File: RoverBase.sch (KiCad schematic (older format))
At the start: 59 parts, among them J1 Conn_01x02, J2 Conn_01x06, J3 Conn_01x04, J4 Conn_01x02, J5 Conn_01x03, J6 Conn_02x03_Counter_Clockwise, J7 Conn_02x03_Counter_Clockwise, SW1 SW_SPDT, SW2 SW_SPDT, SW3 SW_SPDT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

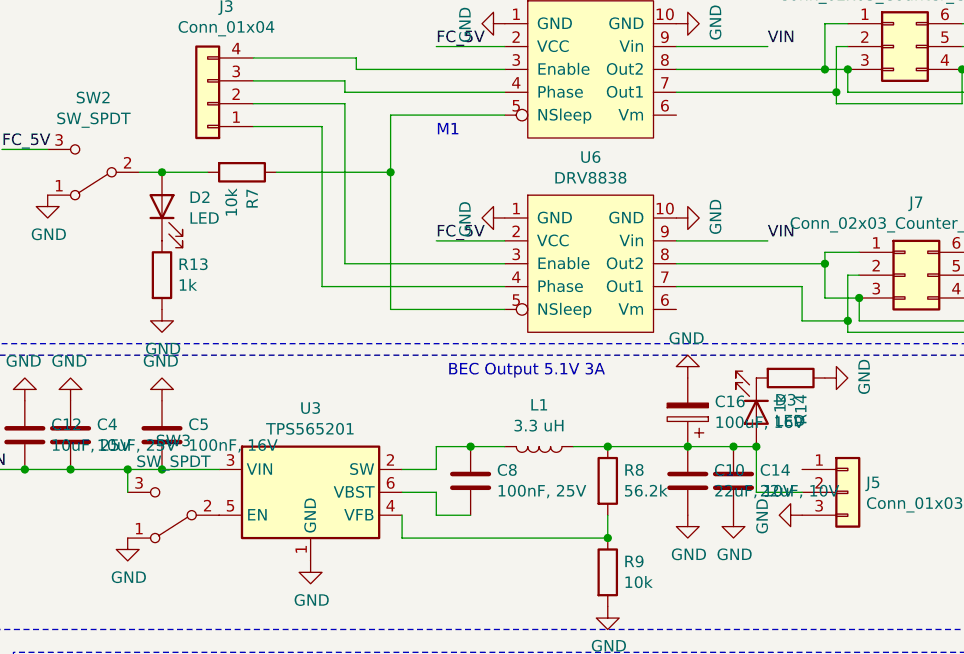
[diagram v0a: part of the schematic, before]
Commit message: Fixes from V1 testing
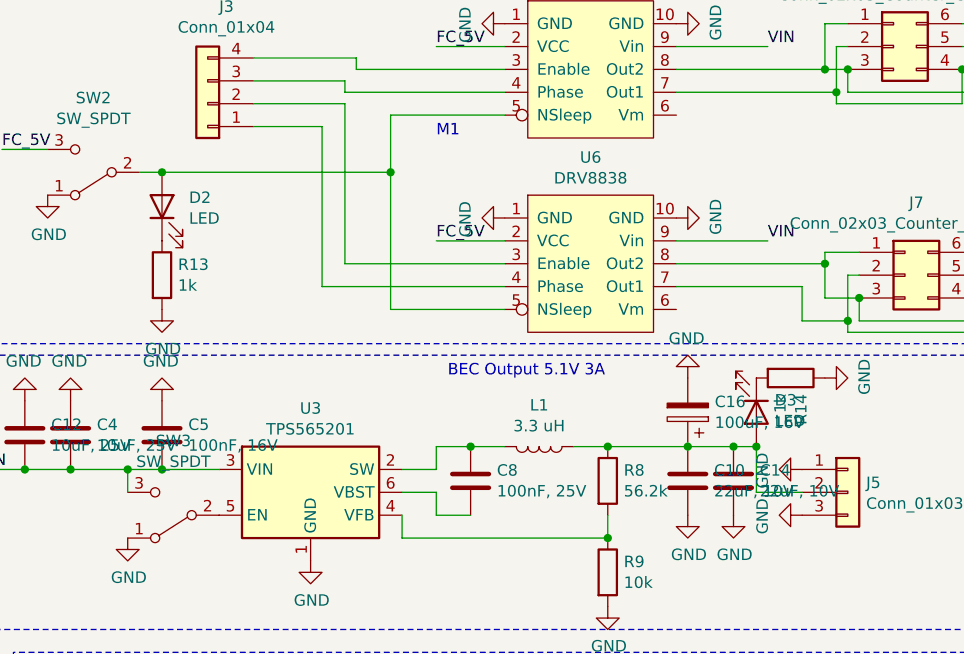
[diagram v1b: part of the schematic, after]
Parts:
- removed R7: 10k, Resistor_SMD:R_0402_1005Metric_Pad0.72x0.64mm_HandSolder, symbol Device:R
- H1, H2, H3, H4: footprint MountingHole:MountingHole_3.2mm_M3_ISO7380 -> MountingHole:MountingHole_3.5mm
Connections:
- net GND: now also J5.1 (Pin_1)
- net at U5.5 (NSleep), U6.5 (NSleep): now also D2.2 (A), SW2.2 (B)
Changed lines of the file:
@@
 Text Notes 3500 1100 0    50   ~ 0
 7A Limit
-$Comp
-L Device:R R7
-U 1 1 5FBF30CD
-P 7900 3900
-F 0 "R7" H 7970 3946 50  0000 L CNN
-F 1 "10k" H 7970 3855 50  0000 L CNN
-F 2 "Resistor_SMD:R_0402_1005Metric_Pad0.72x0.64mm_HandSolder" V 7830 3900 50  0001 C CNN
-F 3 "~" H 7900 3900 50  0001 C CNN
-F 4 "CRCW040210K0FKED" H 7900 3900 50  0001 C CNN "MPN"
-F 5 "541-3959-1-ND" H 7900 3900 50  0001 C CNN "SPN"
-	1    7900 3900
-	0    1    1    0
-$EndComp
 Wire Wire Line
 	8550 3650 8550 3900
 Wire Wire Line
 	7450 3900 7550 3900
-Wire Wire Line
-	8050 3900 8550 3900
 Connection ~ 8550 3900
 Wire Wire Line
@@
 $EndComp
 Connection ~ 7550 3900
-Wire Wire Line
-	7550 3900 7750 3900
 $Comp
 L Device:LED D3
@@
 F 0 "H1" H 1550 6146 50  0000 L CNN
 F 1 "MountingHole" H 1550 6055 50  0000 L CNN
-F 2 "MountingHole:MountingHole_3.2mm_M3_ISO7380" H 1450 6100 50  0001 C CNN
+F 2 "MountingHole:MountingHole_3.5mm" H 1450 6100 50  0001 C CNN
 F 3 "~" H 1450 6100 50  0001 C CNN
 F 4 "nf" H 1450 6100 50  0001 C CNN "MPN"
@@
 F 0 "H3" H 2350 6146 50  0000 L CNN
 F 1 "MountingHole" H 2350 6055 50  0000 L CNN
-F 2 "MountingHole:MountingHole_3.2mm_M3_ISO7380" H 2250 6100 50  0001 C CNN
+F 2 "MountingHole:MountingHole_3.5mm" H 2250 6100 50  0001 C CNN
 F 3 "~" H 2250 6100 50  0001 C CNN
 F 4 "nf" H 2250 6100 50  0001 C CNN "MPN"
@@
 F 0 "H4" H 2350 6546 50  0000 L CNN
 F 1 "MountingHole" H 2350 6455 50  0000 L CNN
-F 2 "MountingHole:MountingHole_3.2mm_M3_ISO7380" H 2250 6500 50  0001 C CNN
+F 2 "MountingHole:MountingHole_3.5mm" H 2250 6500 50  0001 C CNN
 F 3 "~" H 2250 6500 50  0001 C CNN
 F 4 "nf" H 2250 6500 50  0001 C CNN "MPN"
@@
 F 0 "H2" H 1550 6546 50  0000 L CNN
 F 1 "MountingHole" H 1550 6455 50  0000 L CNN
-F 2 "MountingHole:MountingHole_3.2mm_M3_ISO7380" H 1450 6500 50  0001 C CNN
+F 2 "MountingHole:MountingHole_3.5mm" H 1450 6500 50  0001 C CNN
 F 3 "~" H 1450 6500 50  0001 C CNN
 F 4 "nf" H 1450 6500 50  0001 C CNN "MPN"
@@
 	6150 2100 6350 2100
 Connection ~ 6350 2100
+Wire Wire Line
+	7550 3900 8550 3900
+$Comp
+L power:GND #PWR?
+U 1 1 5FFBA6CD
+P 10350 5200
+F 0 "#PWR?" H 10350 4950 50  0001 C CNN
+F 1 "GND" H 10355 5027 50  0000 C CNN
+F 2 "" H 10350 5200 50  0001 C CNN
+F 3 "" H 10350 5200 50  0001 C CNN
+	1    10350 5200
+	0    1    1    0
+$EndComp
 $EndSCHEMATC

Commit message: Updated inductor footprint
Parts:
- L1, L2: footprint Inductor_SMD:L_Vishay_IHLP-4040 -> Vishay_IHLP-3232:L_Vishay_IHLP-3232
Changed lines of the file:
@@
 F 0 "L2" V 9769 1600 50  0000 C CNN
 F 1 "3.3 uH" V 9860 1600 50  0000 C CNN
-F 2 "Inductor_SMD:L_Vishay_IHLP-4040" H 9950 1600 50  0001 C CNN
+F 2 "Vishay_IHLP-3232:L_Vishay_IHLP-3232" H 9950 1600 50  0001 C CNN
 F 3 "~" H 9950 1600 50  0001 C CNN
 F 4 "IHLP3232DZER3R3M01" H 9950 1600 50  0001 C CNN "MPN"
@@
 F 0 "L1" V 9019 5100 50  0000 C CNN
 F 1 "3.3 uH" V 9110 5100 50  0000 C CNN
-F 2 "Inductor_SMD:L_Vishay_IHLP-4040" H 9200 5100 50  0001 C CNN
+F 2 "Vishay_IHLP-3232:L_Vishay_IHLP-3232" H 9200 5100 50  0001 C CNN
 F 3 "~" H 9200 5100 50  0001 C CNN
 F 4 "IHLP3232DZER3R3M01" H 9200 5100 50  0001 C CNN "MPN"

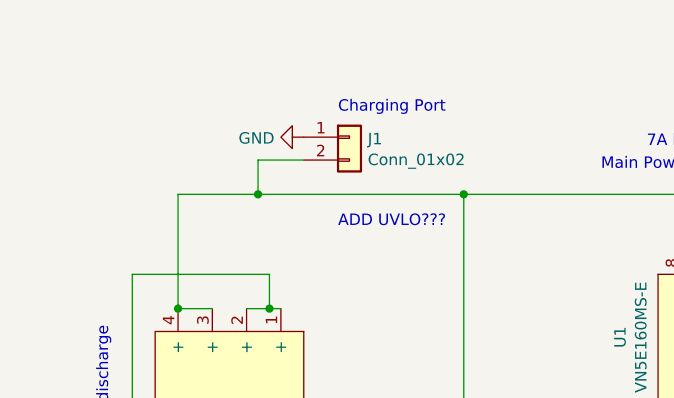
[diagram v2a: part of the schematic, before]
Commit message: Better power supply placement
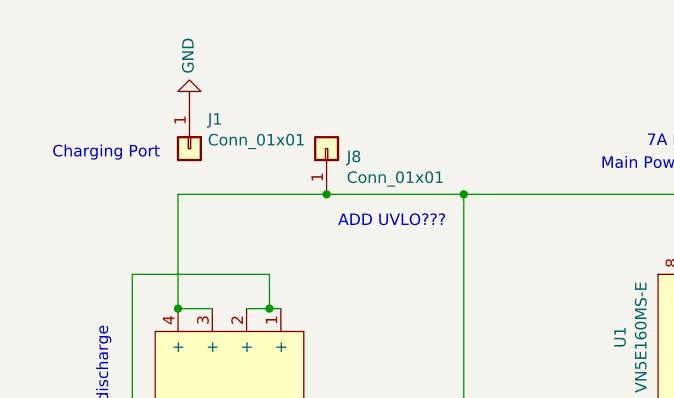
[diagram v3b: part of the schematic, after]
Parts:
- removed J1: Conn_01x02, Connector_PinHeader_2.54mm:PinHeader_1x02_P2.54mm_Vertical, symbol Connector_Generic:Conn_01x02
- added J1, J8: Conn_01x01, Connector_Pin:Pin_D1.3mm_L11.0mm, symbol Connector_Generic:Conn_01x01
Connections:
- net GND: now also J1.1 (Pin_1)
- net at BT1.3 (+), BT1.4 (+), R1.1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: now also J8.1 (Pin_1)
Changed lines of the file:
@@
 $EndDescr
-$Comp
-L Connector_Generic:Conn_01x02 J1
-U 1 1 5F777BC5
-P 2200 1050
-F 0 "J1" H 2280 1042 50  0000 L CNN
-F 1 "Conn_01x02" H 2280 951 50  0000 L CNN
-F 2 "Connector_PinHeader_2.54mm:PinHeader_1x02_P2.54mm_Vertical" H 2200 1050 50  0001 C CNN
-F 3 "~" H 2200 1050 50  0001 C CNN
-F 4 "nf" H 2200 1050 50  0001 C CNN "SPN"
-F 5 "nf" H 2200 1050 50  0001 C CNN "MPN"
-F 6 "dnf" H 2200 1050 50  0001 C CNN "fit_field"
-	1    2200 1050
-	1    0    0    -1
-$EndComp
-Wire Wire Line
-	2000 1150 1800 1150
 $Comp
 L power:GND #PWR02
 U 1 1 5F778348
-P 2000 1050
-F 0 "#PWR02" H 2000 800 50  0001 C CNN
-F 1 "GND" V 2005 922 50  0000 R CNN
-F 2 "" H 2000 1050 50  0001 C CNN
-F 3 "" H 2000 1050 50  0001 C CNN
-	1    2000 1050
-	0    1    1    0
+P 1500 900
+F 0 "#PWR02" H 1500 650 50  0001 C CNN
+F 1 "GND" V 1505 772 50  0000 R CNN
+F 2 "" H 1500 900 50  0001 C CNN
+F 3 "" H 1500 900 50  0001 C CNN
+	1    1500 900
+	-1   0    0    1
 $EndComp
 Text Notes 8750 3750 0    50   ~ 0
@@
 Text Notes 750  3150 0    50   ~ 0
 2x2 18650 Batteries. Thus 7.5-8.5V @ 5000mAh
-Text Notes 2150 950  0    50   ~ 0
+Text Notes 900  1150 0    50   ~ 0
 Charging Port
 $Comp
@@
 	4500 1350 4500 1450
 Wire Wire Line
-	1800 1150 1800 1300
-Wire Wire Line
 	3950 1300 3650 1300
 Connection ~ 3650 1300
@@
 	2700 2650 2700 1300
 Connection ~ 2700 1300
-Wire Wire Line
-	2700 1300 1800 1300
 Wire Wire Line
 	3950 2600 3850 2600
@@
 	1450 2800 1600 2800
 Wire Wire Line
-	1800 1300 1450 1300
-Wire Wire Line
 	1450 1300 1450 1800
-Connection ~ 1800 1300
 Connection ~ 1450 1800
 Wire Wire Line
@@
 	7550 3900 8550 3900
 $Comp
-L power:GND #PWR?
+L power:GND #PWR0104
 U 1 1 5FFBA6CD
 P 10350 5200
-F 0 "#PWR?" H 10350 4950 50  0001 C CNN
+F 0 "#PWR0104" H 10350 4950 50  0001 C CNN
 F 1 "GND" H 10355 5027 50  0000 C CNN
 F 2 "" H 10350 5200 50  0001 C CNN
@@
 	0    1    1    0
 $EndComp
+$Comp
+L Connector_Generic:Conn_01x01 J8
+U 1 1 5FF9B4C5
+P 2100 1100
+F 0 "J8" V 2064 1012 50  0000 R CNN
+F 1 "Conn_01x01" V 1973 1012 50  0000 R CNN
+F 2 "Connector_Pin:Pin_D1.3mm_L11.0mm" H 2100 1100 50  0001 C CNN
+F 3 "~" H 2100 1100 50  0001 C CNN
+	1    2100 1100
+	0    -1   -1   0
+$EndComp
+$Comp
+L Connector_Generic:Conn_01x01 J1
+U 1 1 5FF9D287
+P 1500 1100
+F 0 "J1" V 1372 1180 50  0000 L CNN
+F 1 "Conn_01x01" V 1463 1180 50  0000 L CNN
+F 2 "Connector_Pin:Pin_D1.3mm_L11.0mm" H 1500 1100 50  0001 C CNN
+F 3 "~" H 1500 1100 50  0001 C CNN
+	1    1500 1100
+	0    1    1    0
+$EndComp
+Connection ~ 2100 1300
+Wire Wire Line
+	2100 1300 2700 1300
+Wire Wire Line
+	1450 1300 2100 1300
 $EndSCHEMATC

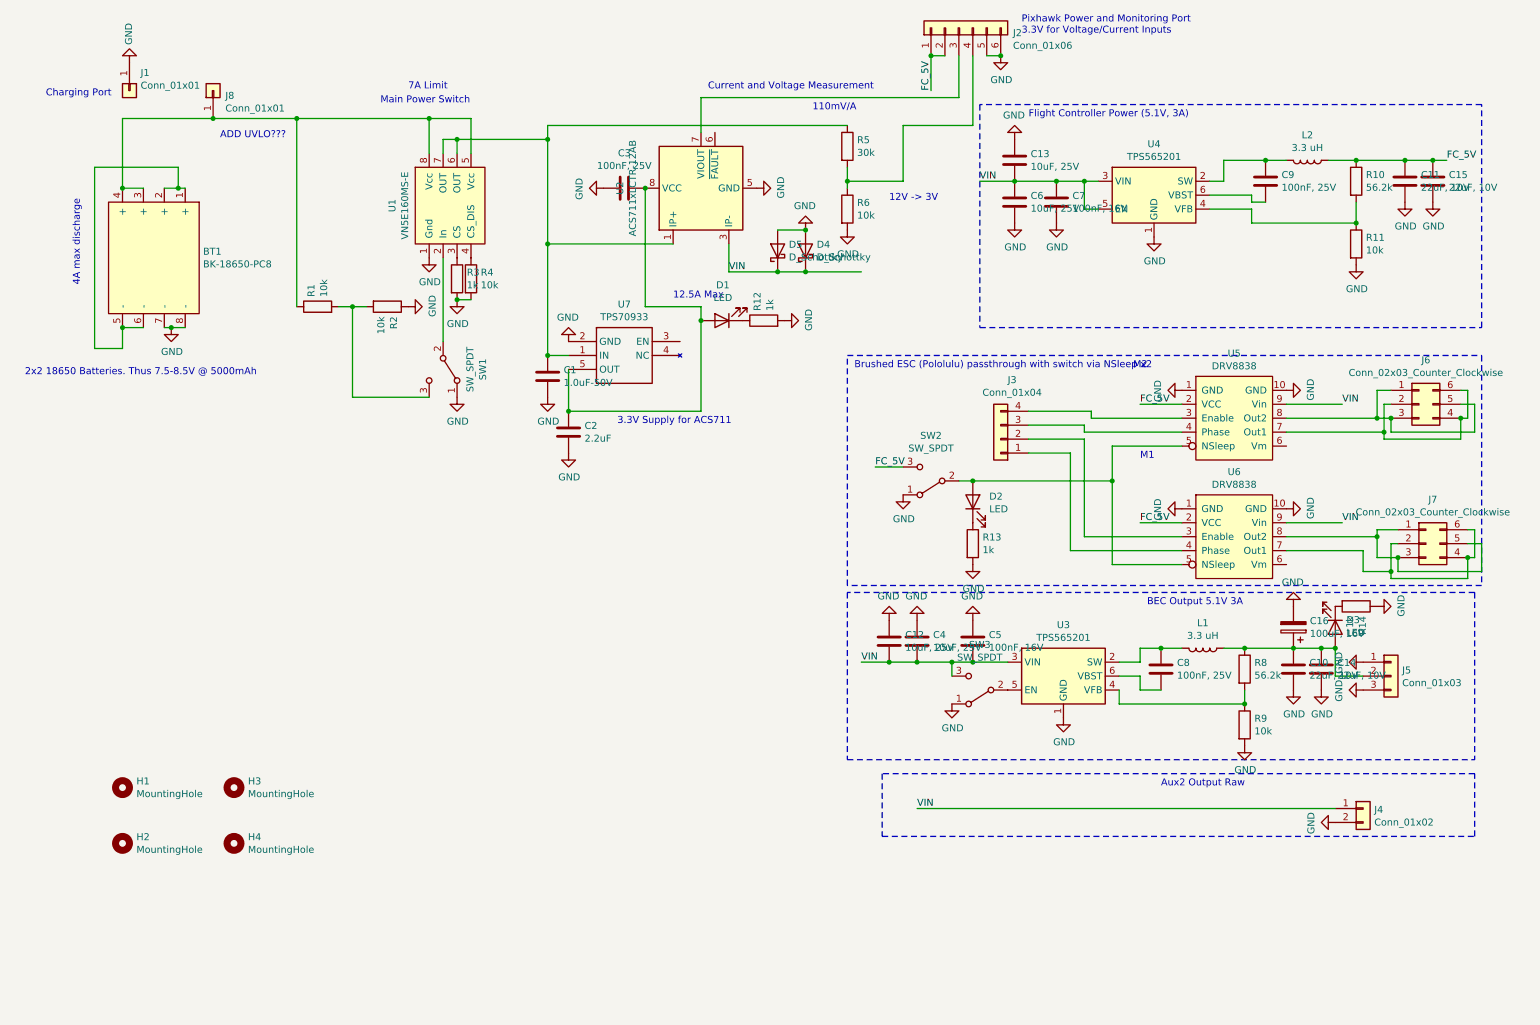
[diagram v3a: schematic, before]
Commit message: Updated motor controllers
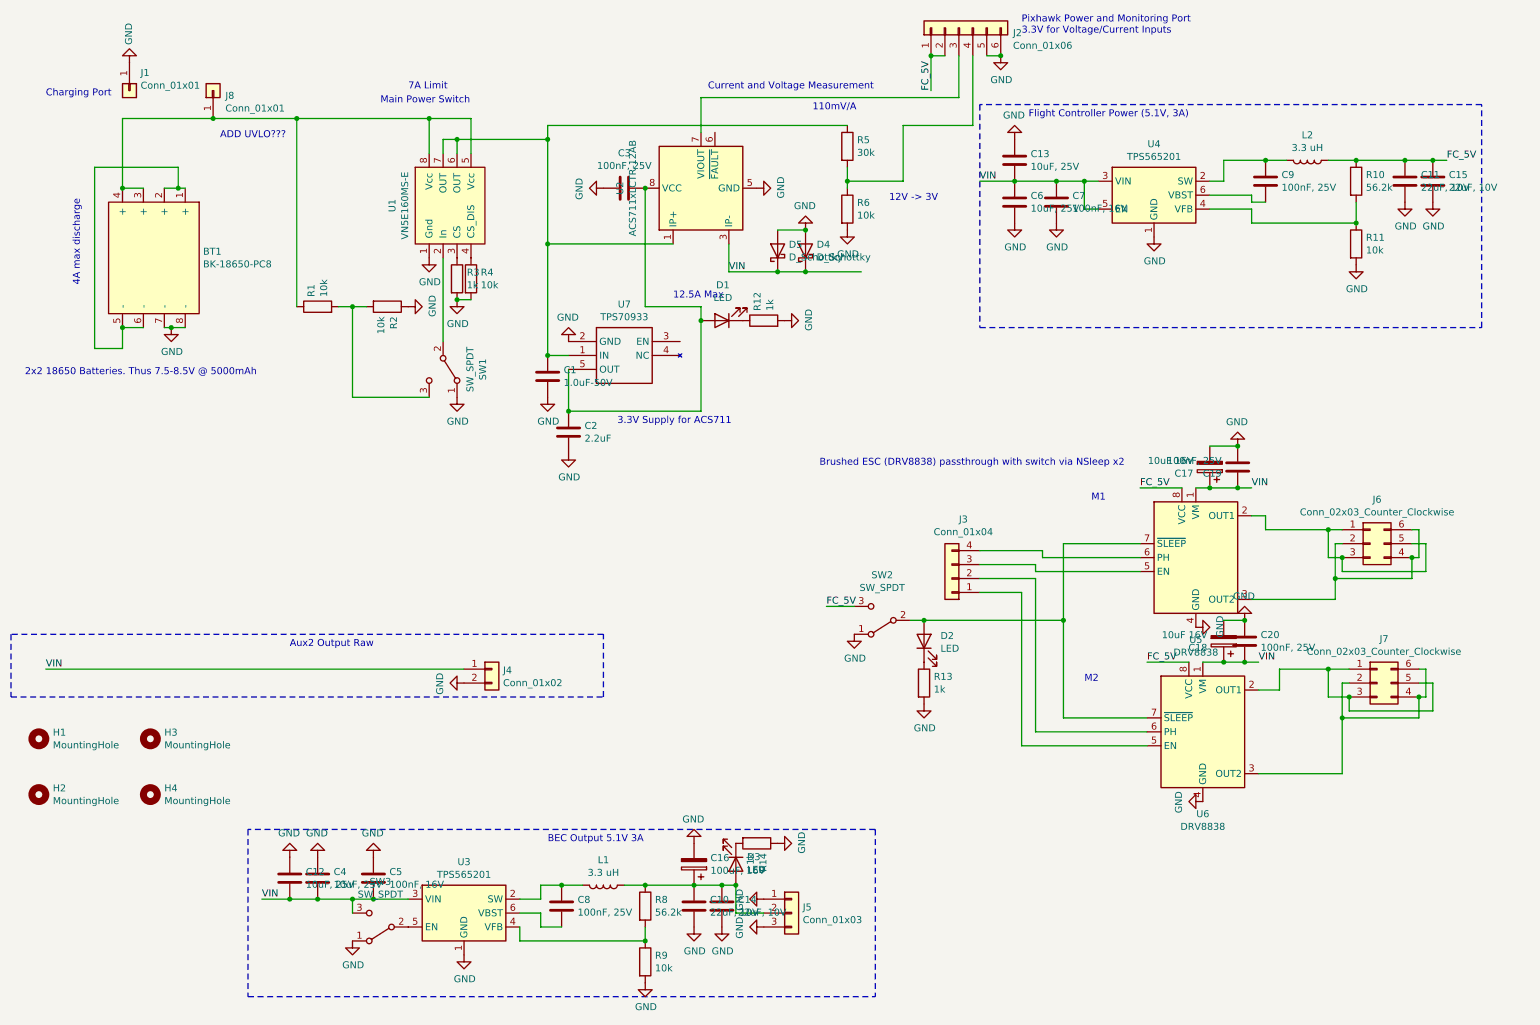
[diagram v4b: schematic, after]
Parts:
- removed U5, U6: DRV8838, Package_DIP:DIP-10_W7.62mm_LongPads, symbol Pololu:DRV8838
- added C17, C18: 10uF 16V, Capacitor_SMD:CP_Elec_4x5.4, symbol Device:CP
- added C19, C20: 100nF, 25V, Capacitor_SMD:C_0603_1608Metric, symbol Device:C
- added U5, U6: DRV8838, Package_SON:WSON-8-1EP_2x2mm_P0.5mm_EP0.9x1.6mm, symbol Driver_Motor:DRV8838
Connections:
- net FC_5V: now also U5.8 (VCC), U6.8 (VCC)
- net GND: now also C17.2, C18.2, C19.2, C20.1, U5.4 (GND), U5.9 (GND), U6.4 (GND), U6.9 (GND)
- net VIN: now also C17.1, C18.1, C19.1, C20.2, U5.1 (VM), U6.1 (VM)
- net at J3.4 (Pin_4): now also U5.6 (PH)
- net at J3.3 (Pin_3): now also U5.5 (EN)
- net at D2.2 (A), SW2.2 (B): now also U5.7 (~SLEEP), U6.7 (~SLEEP)
- net at J6.2 (Pin_2), J6.4 (Pin_4), J6.6 (Pin_6): now also U5.3 (OUT2)
- net at J6.1 (Pin_1), J6.3 (Pin_3), J6.5 (Pin_5): now also U5.2 (OUT1)
- net at J3.2 (Pin_2): now also U6.6 (PH)
- net at J3.1 (Pin_1): now also U6.5 (EN)
- net at J7.2 (Pin_2), J7.4 (Pin_4), J7.6 (Pin_6): now also U6.3 (OUT2)
- net at J7.1 (Pin_1), J7.3 (Pin_3), J7.5 (Pin_5): now also U6.2 (OUT1)
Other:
- note added: "Brushed ESC (DRV8838) passthrough with switch via NSleep x2"
- note removed: "Brushed ESC (Pololulu) passthrough with switch via NSleep x2"
- moved on the sheet: C10, C12, C14, C16, C4, C5, C8, D2, D3, H1, H2, H3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

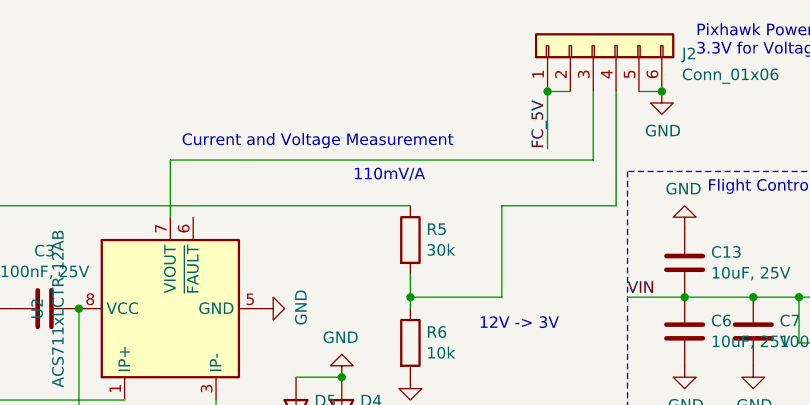
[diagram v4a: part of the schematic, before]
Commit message: Smaller size pcb and re-layout
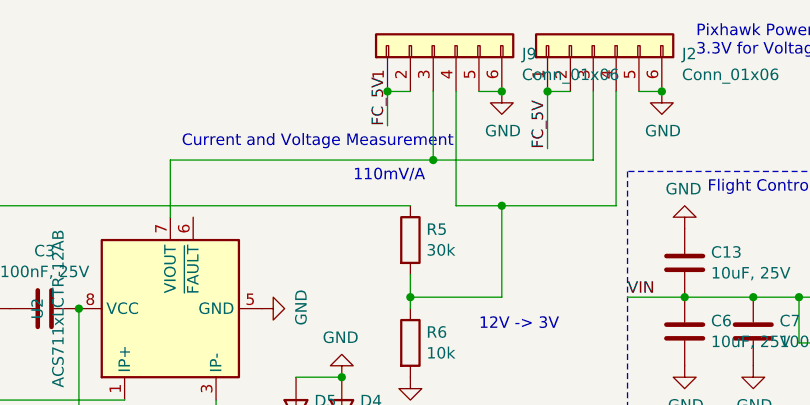
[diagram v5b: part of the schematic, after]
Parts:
- added J9: Conn_01x06, Connector_PinHeader_2.54mm:PinHeader_1x06_P2.54mm_Vertical, symbol Connector_Generic:Conn_01x06
- J2: footprint Connector_JST:JST_GH_SM06B-GHS-TB_1x06-1MP_P1.25mm_Horizontal -> Connector_JST:JST_GH_BM06B-GHS-TBT_1x06-1MP_P1.25mm_Vertical; MPN SM06B-GHS-TB(LF)(SN) -> (none); SPN 455-1568-1-ND -> (none)
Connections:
- net FC_5V: now also J9.1 (Pin_1), J9.2 (Pin_2)
- net GND: now also J9.5 (Pin_5), J9.6 (Pin_6)
- net at J2.3 (Pin_3), U2.7 (VIOUT): now also J9.3 (Pin_3)
- net at J2.4 (Pin_4), R5.2, R6.1: now also J9.4 (Pin_4)
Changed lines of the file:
@@
 F 0 "J2" V 7414 262 50  0000 R CNN
 F 1 "Conn_01x06" V 7323 262 50  0000 R CNN
-F 2 "Connector_JST:JST_GH_SM06B-GHS-TB_1x06-1MP_P1.25mm_Horizontal" H 7450 650 50  0001 C CNN
+F 2 "Connector_JST:JST_GH_BM06B-GHS-TBT_1x06-1MP_P1.25mm_Vertical" H 7450 650 50  0001 C CNN
 F 3 "~" H 7450 650 50  0001 C CNN
-F 4 "SM06B-GHS-TB(LF)(SN)" H 7450 650 50  0001 C CNN "MPN"
-F 5 "455-1568-1-ND" H 7450 650 50  0001 C CNN "SPN"
+F 4 "" H 7450 650 50  0001 C CNN "MPN"
+F 5 "" H 7450 650 50  0001 C CNN "SPN"
 	1    7450 650
 	0    -1   -1   0
@@
 	7450 850  7450 1150
 Wire Wire Line
-	7450 1150 5600 1150
+	7450 1150 6750 1150
 $Comp
 L Regulator_Switching:TPS565208 U4
@@
 	9250 3650 9450 3650
 Connection ~ 9450 3650
+$Comp
+L Connector_Generic:Conn_01x06 J9
+U 1 1 6022697D
+P 6750 650
+F 0 "J9" V 6714 262 50  0000 R CNN
+F 1 "Conn_01x06" V 6623 262 50  0000 R CNN
+F 2 "Connector_PinHeader_2.54mm:PinHeader_1x06_P2.54mm_Vertical" H 6750 650 50  0001 C CNN
+F 3 "~" H 6750 650 50  0001 C CNN
+F 4 "" H 6750 650 50  0001 C CNN "MPN"
+F 5 "" H 6750 650 50  0001 C CNN "SPN"
+	1    6750 650
+	0    -1   -1   0
+$EndComp
+Wire Wire Line
+	6950 850  7050 850
+Wire Wire Line
+	6550 850  6650 850
+Wire Wire Line
+	6750 850  6750 1150
+Connection ~ 6750 1150
+Wire Wire Line
+	6750 1150 5600 1150
+Wire Wire Line
+	6850 850  6850 1350
+Wire Wire Line
+	6850 1350 7050 1350
+Connection ~ 7050 1350
+Wire Wire Line
+	6550 850  6550 1000
+Connection ~ 6550 850
+$Comp
+L power:GND #PWR0107
+U 1 1 60254ABC
+P 7050 850
+F 0 "#PWR0107" H 7050 600 50  0001 C CNN
+F 1 "GND" H 7055 677 50  0000 C CNN
+F 2 "" H 7050 850 50  0001 C CNN
+F 3 "" H 7050 850 50  0001 C CNN
+	1    7050 850
+	1    0    0    -1
+$EndComp
+Connection ~ 7050 850
+Text Label 6550 1000 1    50   ~ 0
+FC_5V
 $EndSCHEMATC
